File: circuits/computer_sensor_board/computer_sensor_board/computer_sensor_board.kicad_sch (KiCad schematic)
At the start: 8 parts, among them J1 Conn_Jetson, J2 Conn_Main_ADC, J3 USB_M5Stack_0, J4 USB_M5Stack_1, U1 TDN_5-2411WISM, U2 Teensy4.1

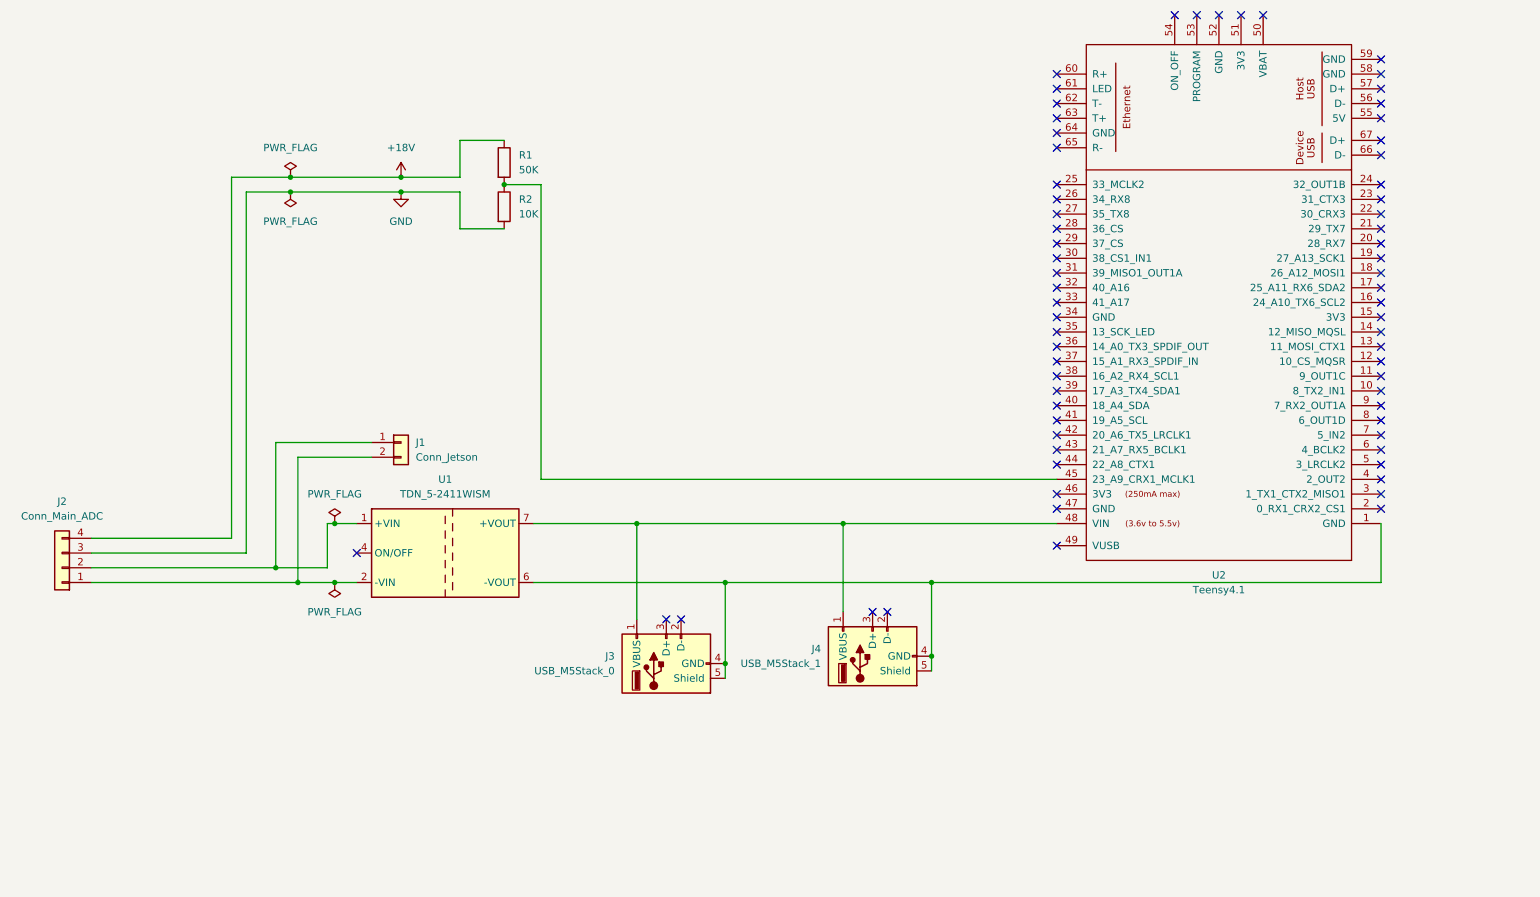
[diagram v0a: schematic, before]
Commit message: rename project
Signed-off-by: Masaya Kataoka <ms.kataoka@gmail.com>
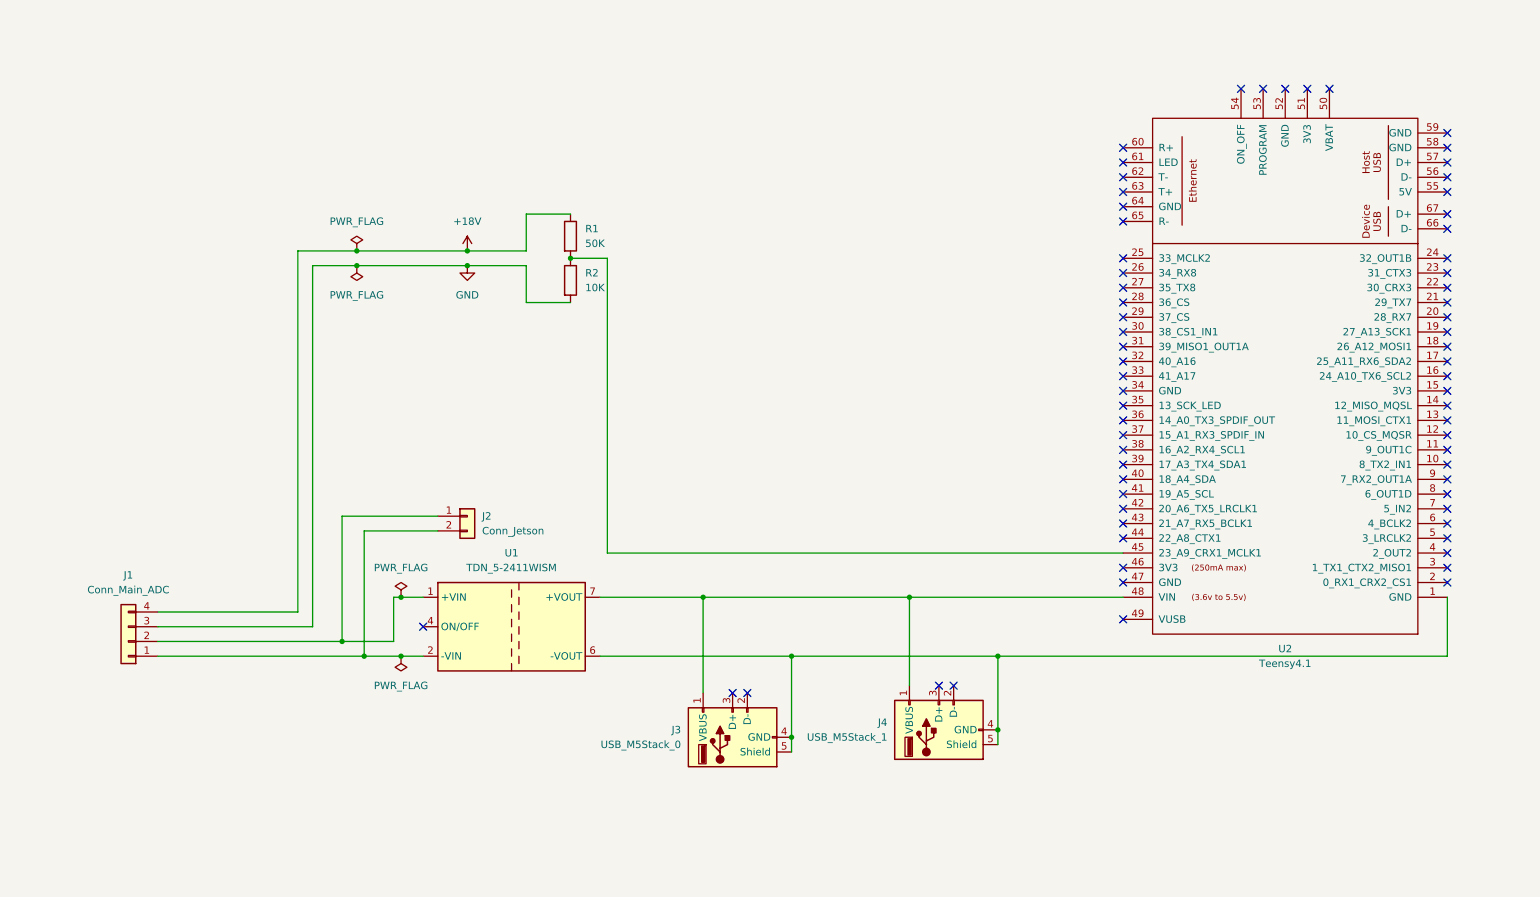
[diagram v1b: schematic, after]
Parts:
- removed J1: Conn_Jetson, symbol Connector_Generic:Conn_01x02
- removed J2: Conn_Main_ADC, symbol Connector_Generic:Conn_01x04
- added J1: Conn_Main_ADC, symbol Connector_Generic:Conn_01x04
- added J2: Conn_Jetson, symbol Connector_Generic:Conn_01x02
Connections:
- net +18V: now also J1.4 (Pin_4)
- net GND: now also J1.3 (Pin_3)
- net at U1.1 (+VIN): now also J1.2 (Pin_2), J2.1 (Pin_1)
- net at U1.2 (-VIN): now also J1.1 (Pin_1), J2.2 (Pin_2)

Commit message: Fix/add ad converter (#356)
* add start script

Signed-off-by: Masaya Kataoka <ms.kataoka@gmail.com>

* add BOM plugin

Signed-off-by: Masaya Kataoka <ms.kataoka@gmail.com>

* enable use x11 forwarding

Signed-off-by: Masaya Kataoka <ms.kataoka@gmail.com>

* update description

Signed-off-by: Masaya Kataoka <ms.kataoka@gmail.com>

* update Dockerfile

Signed-off-by: Masaya Kataoka <ms.kataoka@gmail.com>

* add 3rd party directory

Signed-off-by: Masaya Kataoka <ms.kataoka@gmail.com>

* add entrypoint.sh

Signed-off-by: Masaya Kataoka <ms.kataoka@gmail.com>

* add teensy library

Signed-off-by: Masaya Kataoka <ms.kataoka@gmail.com>

* add teensy

Signed-off-by: Masaya Kataoka <ms.kataoka@gmail.com>

* enable run kibot

Signed-off-by: Masaya Kataoka <ms.kataoka@gmail.com>

* update kibot.yaml

Signed-off-by: Masaya Kataoka <ms.kataoka@gmail.com>

* enable save schematic in SVG

Signed-off-by: Masaya Kataoka <ms.kataoka@gmail.com>

* rename project

Signed-off-by: Masaya Kataoka <ms.kataoka@gmail.com>

* add SVG schematic

Signed-off-by: Masaya Kataoka <ms.kataoka@gmail.com>

* enable show schematics

Signed-off-by: Masaya Kataoka <ms.kataoka@gmail.com>

* fix dashboard

Signed-off-by: Masaya Kataoka <ms.kataoka@gmail.com>

* add depends

Signed-off-by: Masaya Kataoka <ms.kataoka@gmail.com>

* use uv

Signed-off-by: Masaya Kataoka <ms.kataoka@gmail.com>

* fix typo

Signed-off-by: Masaya Kataoka <ms.kataoka@gmail.com>

* update schematics

Signed-off-by: Masaya Kataoka <ms.kataoka@gmail.com>

* add AD converter

Signed-off-by: Masaya Kataoka <ms.kataoka@gmail.com>

* add run kibot step

Signed-off-by: Masaya Kataoka <ms.kataoka@gmail.com>

---------

Signed-off-by: Masaya Kataoka <ms.kataoka@gmail.com>
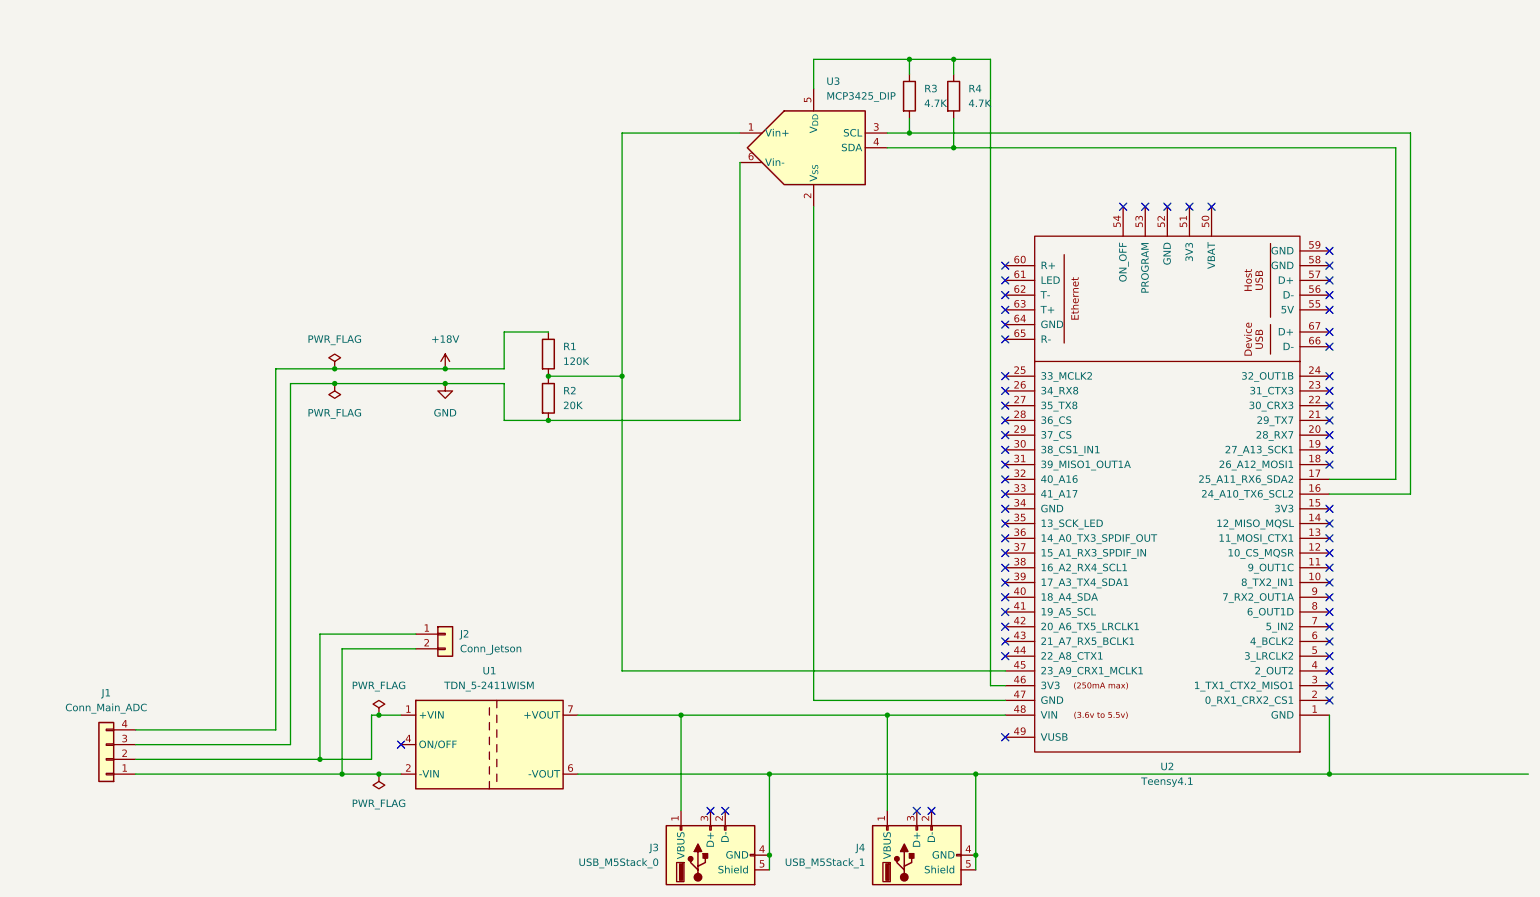
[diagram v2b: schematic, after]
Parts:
- added R3, R4: 4.7K, symbol Device:R
- added U3: MCP3425_DIP, Package_TO_SOT_SMD:SOT-23-6, symbol Analog_ADC:MCP3425Axx-xCH
- R1: value 50K -> 120K
- R2: value 10K -> 20K
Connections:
- net GND: now also U3.6 (Vin-)
- net at U2.16 (24_A10_TX6_SCL2): now also R3.2, U3.3 (SCL)
- net at U2.17 (25_A11_RX6_SDA2): now also R4.2, U3.4 (SDA)
- net at R1.2, R2.1, U2.45 (23_A9_CRX1_MCLK1): now also U3.1 (Vin+)
- net at U2.46 (3V3): now also R3.1, R4.1, U3.5 (V_{DD})
- net at U2.47 (GND): now also U3.2 (V_{SS})
- no-connect marks 69 -> 65
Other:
- moved on the sheet: J1, J2, J3, J4, R1, R2, U1, U2
